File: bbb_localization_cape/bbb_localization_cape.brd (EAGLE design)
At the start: 71.8 x 54.6 mm, 33 parts, among them J2 MOLEX-22-03-5035, U1 SN65HVD256DR, U2 ARDUCAMOV5642, U3 SN74LV1T126DCKR, U4 MSP430G2553IPW20R, U5 SN74LV1T125DCKR, U6 LP38693MP-3.3/NOPB, U7 LM1085ISX-ADJ

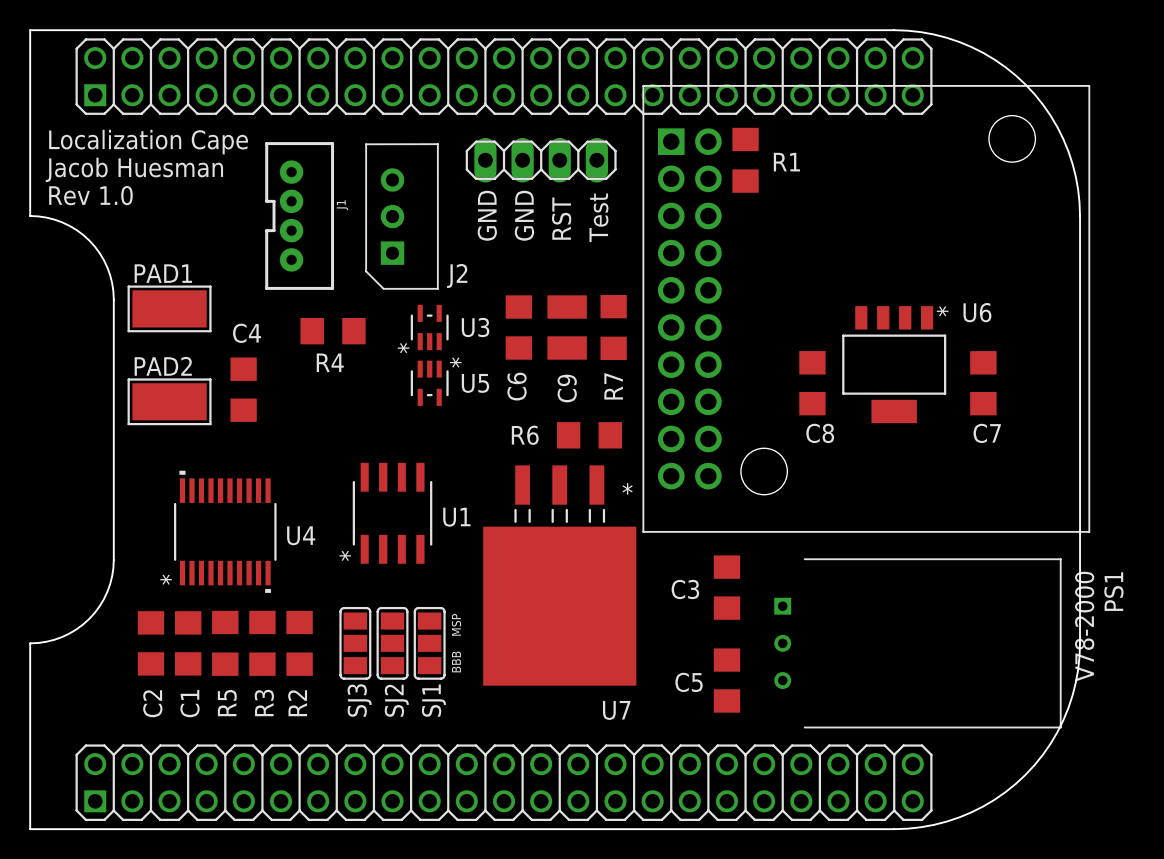
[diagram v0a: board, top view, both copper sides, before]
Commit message: Create ground plane
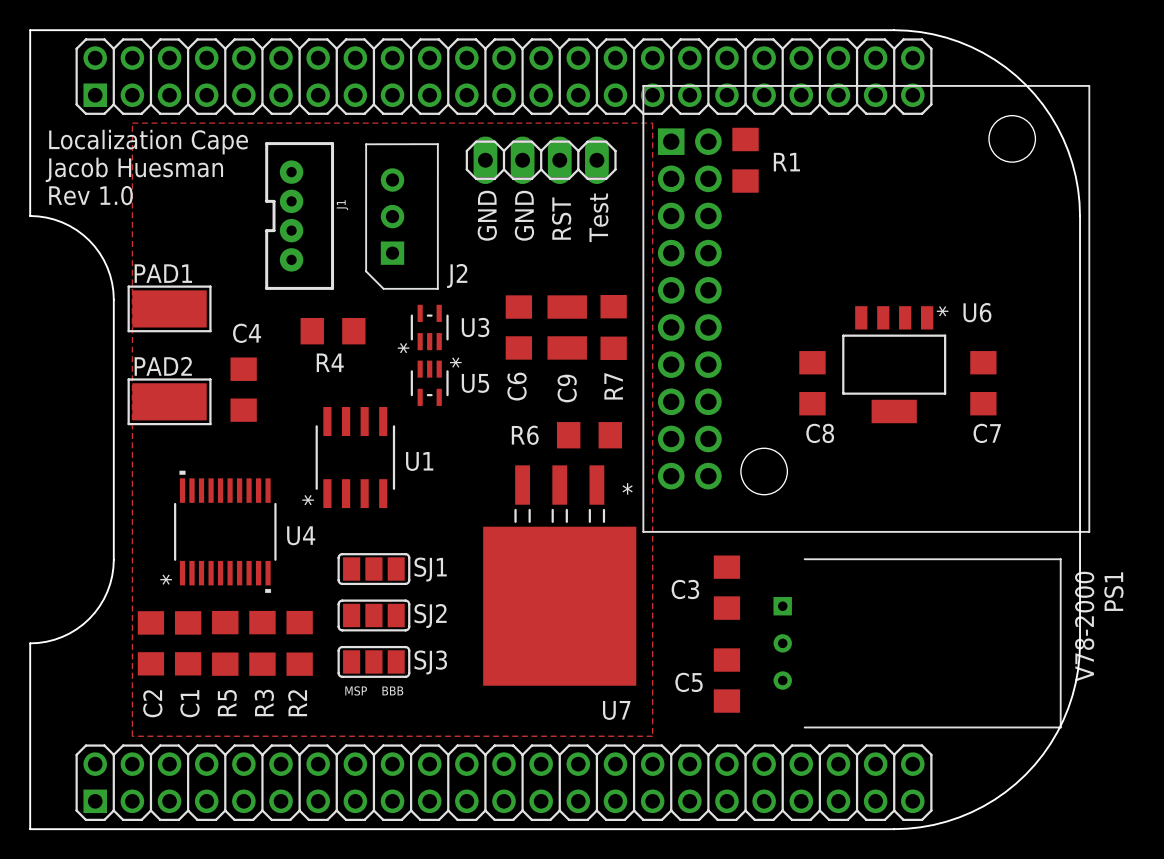
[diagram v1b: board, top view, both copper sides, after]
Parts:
- moved SJ1 6.35 mm to (38.1, 17.8), turned to 0 degrees
- moved U1 4.58 mm to (36.8, 25.4)
- moved SJ2 2.29 mm to (38.1, 14.6), turned to 0 degrees
- moved SJ3 1.80 mm to (38.1, 11.4), turned to 0 degrees
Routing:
- added copper zone on layer 1, net GND

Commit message: Laid out power connections
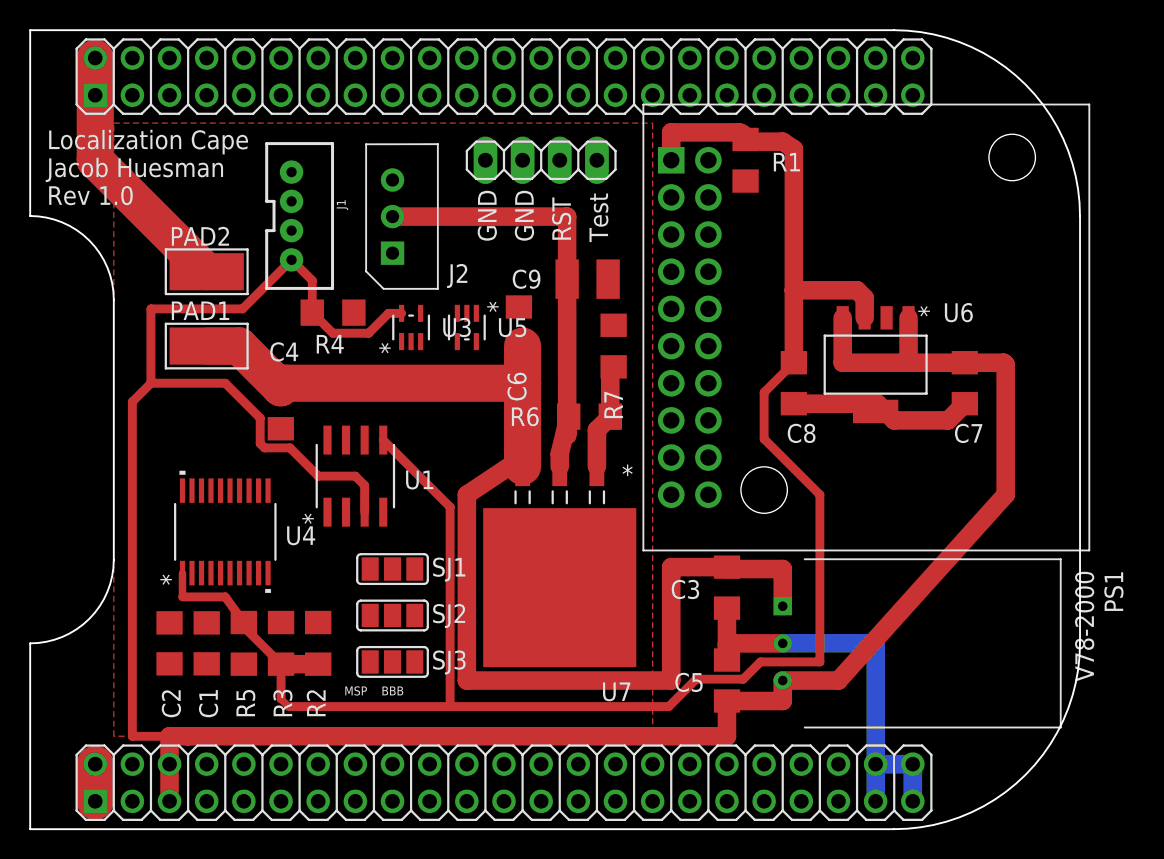
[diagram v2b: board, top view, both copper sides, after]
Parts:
- moved PAD2 9.25 mm to (26.7, 38.1)
- moved U5 4.58 mm to (44.5, 34.3)
- moved PAD1 3.59 mm to (26.7, 33.0)
- moved C9 3.59 mm to (52.7, 37.6), turned to 0 degrees
- moved C4 2.84 mm to (31.7, 28.8)
- moved C1 1.27 mm to (26.7, 12.7)
- moved U2 1.27 mm to (58.4, 45.7)
- moved U7 1.27 mm to (50.8, 16.5)
- moved C2 1.27 mm to (24.1, 12.7)
- moved R3 1.27 mm to (31.8, 12.7)
- moved R5 1.27 mm to (29.2, 12.7)
- moved R6 1.27 mm to (52.8, 28.2)
- moved U1 1.27 mm to (36.8, 24.1)
- moved C7 1.27 mm to (78.5, 30.5)
- moved C8 1.27 mm to (66.8, 30.5)
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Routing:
- net +5V: track 0.00 -> 173.6 mm
- net +3V3: track 0.00 -> 128.6 mm
- net +12V: track 0.00 -> 80.4 mm
- net GND: track 0.00 -> 63.7 mm
- net +10V: track 0.00 -> 31.6 mm
- net N$3: track 0.00 -> 7.28 mm

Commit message: Finished board layout
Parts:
- moved R1 17.5 mm to (79.7, 39.1), turned to 0 degrees
- moved C7 3.81 mm to (82.3, 30.5)
- moved U6 3.81 mm to (76.2, 31.8)
- moved C8 3.81 mm to (70.6, 30.5)
- moved R7 1.27 mm to (55.8, 33.0)
- renumbered PAD1 to GND, PAD2 to +12V
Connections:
- new net N$4: C7.2, C8.2, U6.5
- net GND: no longer C7.2, C8.2, U6.5
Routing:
- net GND: track 63.7 -> 174.7 mm, vias 0 -> 8
- net I2C_SDA: track 0.00 -> 92.1 mm, vias 0 -> 3
- net I2C2_SCL: track 0.00 -> 78.7 mm, vias 0 -> 2
- net RST: track 0.00 -> 73.8 mm, vias 0 -> 3
- net DCAN1_TX: track 0.00 -> 53.1 mm, vias 0 -> 1
- net TEST: track 0.00 -> 52.0 mm, vias 0 -> 2
- net TIMER4: track 0.00 -> 50.3 mm
- net +3V3: track 128.6 -> 178.6 mm
- net PRU1_1: track 0.00 -> 37.3 mm
- net PRU1_0: track 0.00 -> 33.1 mm
- net PWDN: track 0.00 -> 32.6 mm
- net PRU1_3: track 0.00 -> 31.6 mm
- net PRU1_6: track 0.00 -> 29.2 mm, vias 0 -> 1
- net UART_DYN_RXD: track 0.00 -> 28.8 mm, vias 0 -> 2
- net PRU1_5: track 0.00 -> 28.0 mm
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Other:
- board text added: "Localization Cape Rev 1.0 JH"
- board text removed: "Localization Cape Jacob Huesman Rev 1.0"

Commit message: Fixed issues between board and schematic, had to ripup the board
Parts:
- moved +12V 5.08 mm to (26.7, 33.0)
- moved GND 5.08 mm to (26.7, 38.1)
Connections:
- removed net I2C2_SCL: A1.65, R1.1, U2.3
- removed net N$4: C7.2, C8.2, U6.5
- removed net TAB: U7.4
- net +10V: now also U7.4
- net +12V: now also +12V.1; no longer GND.1
- net GND: now also C7.2, C8.2, GND.1, U6.5; no longer +12V.1
- net I2C_SCL: now also A1.65, R1.1, U2.3
- net PRU1_12: now also A1.21
- net UART2_DIR: now also A1.69
- net UART_MSP_DIR: now also U4.8
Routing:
- net +3V3: track 178.6 -> 0.00 mm
- net +5V: track 176.4 -> 0.00 mm
- net GND: track 174.7 -> 0.00 mm, vias 8 -> 0
- net I2C_SDA: track 92.1 -> 0.00 mm, vias 3 -> 0
- net +12V: track 80.8 -> 0.00 mm
- net I2C2_SCL: track 78.7 -> 0.00 mm, vias 2 -> 0
- net RST: track 73.8 -> 0.00 mm, vias 3 -> 0
- net DCAN1_TX: track 53.1 -> 0.00 mm, vias 1 -> 0
- net TEST: track 52.0 -> 0.00 mm, vias 2 -> 0
- net TIMER4: track 50.3 -> 0.00 mm
- net PRU1_1: track 37.3 -> 0.00 mm
- net PRU1_0: track 33.1 -> 0.00 mm
- net PWDN: track 32.6 -> 0.00 mm
- net +10V: track 31.6 -> 0.00 mm
- net PRU1_3: track 31.6 -> 0.00 mm
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
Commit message: Cleaned up beaglebone_outline schematic symbol
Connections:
- net I2C_SCL renamed I2C2_SCL
- net I2C_SDA renamed I2C2_SDA
- net SYS_5V renamed 07.SYS_5V
- removed net AIN0: A1.85
- removed net VDD_3V3EXP: A1.49, A1.50
- new net 03.VDD_3V3: A1.49
- new net GNDA_ADC.34: A1.80
- new net SYS_5V.08: A1.54
- new net VDD_3V3.04: A1.50
- new net VDD_ADC.32: A1.78
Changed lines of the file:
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@@
 <signals>
 <signal name="SYS_5V">
-<contactref element="A1" pad="53"/>
 </signal>
 <signal name="AIN0">
-<contactref element="A1" pad="85"/>
 </signal>
 <signal name="GND">
@@
 <contactref element="JP1" pad="4"/>
 <contactref element="JP1" pad="3"/>
-<contactref element="A1" pad="89"/>
-<contactref element="A1" pad="90"/>
-<contactref element="A1" pad="91"/>
-<contactref element="A1" pad="92"/>
-<contactref element="A1" pad="1"/>
-<contactref element="A1" pad="2"/>
 <contactref element="U1" pad="2"/>
 <contactref element="J1" pad="1"/>
@@
 <contactref element="U6" pad="5"/>
 <contactref element="C8" pad="2"/>
+<contactref element="A1" pad="1"/>
+<contactref element="A1" pad="2"/>
+<contactref element="A1" pad="89"/>
+<contactref element="A1" pad="91"/>
+<contactref element="A1" pad="90"/>
+<contactref element="A1" pad="92"/>
 <wire x1="76.2" y1="28.5496" x2="82.296" y2="29.08" width="0" layer="19" extent="1-1"/>
 <wire x1="70.612" y1="29.08" x2="76.2" y2="28.5496" width="0" layer="19" extent="1-1"/>
@@
 <wire x1="49.53" y1="4.445" x2="34.925" y2="21.6662" width="0" layer="19" extent="1-1"/>
 </signal>
-<signal name="I2C_SDA">
+<signal name="I2C2_SDA">
 <contactref element="A1" pad="66"/>
 <contactref element="U4" pad="15"/>
@@
 </signal>
 <signal name="VDD_3V3EXP">
-<contactref element="A1" pad="49"/>
-<contactref element="A1" pad="50"/>
-<wire x1="21.59" y1="1.905" x2="21.59" y2="4.445" width="0" layer="19" extent="1-1"/>
 </signal>
 <signal name="PRU1_8">
@@
 <wire x1="24.13" y1="11.3" x2="29.21" y2="11.278" width="0" layer="19" extent="1-1"/>
 </signal>
-<signal name="I2C_SCL">
+<signal name="I2C2_SCL">
 <contactref element="U4" pad="14"/>
 <contactref element="A1" pad="65"/>
@@
 <wire x1="36.195" y1="26.5938" x2="32.47" y2="40.91" width="0" layer="19" extent="1-1"/>
 </signal>
+<signal name="03.VDD_3V3">
+<contactref element="A1" pad="49"/>
+</signal>
+<signal name="07.SYS_5V">
+<contactref element="A1" pad="53"/>
+</signal>
+<signal name="39">
+</signal>
+<signal name="VDD_3V3.04">
+<contactref element="A1" pad="50"/>
+</signal>
+<signal name="SYS_5V.08">
+<contactref element="A1" pad="54"/>
+</signal>
+<signal name="VDD_ADC.32">
+<contactref element="A1" pad="78"/>
+</signal>
+<signal name="GNDA_ADC.34">
+<contactref element="A1" pad="80"/>
+</signal>
 </signals>

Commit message: Went over the entire schematic
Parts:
- removed C1: 100nF, resistor:C1206
- removed R3: 47k, resistor:R1206
- J2: device bbb_cape_parts:MOLEX-22-03-5035 -> bbb_localization_cape:MOLEX-22-03-5035
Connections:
- removed net N$7: C1.1, R3.1, U4.5
- net +3V3: no longer R3.2
- net GND: no longer C1.2
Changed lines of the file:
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@@
 <attribute name="VENDOR" value="Texas Instruments" x="27.94" y="20.32" size="1.778" layer="27" rot="R90" display="off"/>
-</element>
-<element name="R3" library="resistor" library_urn="urn:adsk.eagle:library:348" package="R1206" package3d_urn="urn:adsk.eagle:package:26062/1" value="47k" x="31.75" y="12.7" smashed="yes" rot="R270">
-<attribute name="NAME" x="31.242" y="9.652" size="1.27" layer="25" rot="R270"/>
-</element>
-<element name="C1" library="resistor" library_urn="urn:adsk.eagle:library:348" package="C1206" package3d_urn="urn:adsk.eagle:package:26140/1" value="100nF" x="26.67" y="12.7" smashed="yes" rot="R90">
-<attribute name="NAME" x="26.162" y="9.652" size="1.27" layer="25" rot="R270"/>
 </element>
 <element name="R5" library="resistor" library_urn="urn:adsk.eagle:library:348" package="R1206" package3d_urn="urn:adsk.eagle:package:26062/1" value="47k" x="29.21" y="12.7" smashed="yes" rot="R90">
@@
 <attribute name="NAME" x="34.036" y="32.512" size="1.27" layer="25"/>
 </element>
-<element name="J2" library="bbb_cape_parts" package="MOLEX-22-03-5035" value="MOLEX-22-03-5035" x="39.37" y="39.37" smashed="yes" rot="R90">
+<element name="J2" library="bbb_localization_cape" package="MOLEX-22-03-5035" value="MOLEX-22-03-5035" x="39.37" y="39.37" smashed="yes" rot="R90">
 <attribute name="NAME" x="43.18" y="37.338" size="1.27" layer="25"/>
 </element>
@@
 <contactref element="C9" pad="2"/>
 <contactref element="C6" pad="2"/>
-<contactref element="C1" pad="2"/>
 <contactref element="U4" pad="20"/>
 <contactref element="C2" pad="2"/>
@@
 <wire x1="25.015003125" y1="23.1394" x2="31.73415" y2="27.36826875" width="0" layer="19" extent="1-1"/>
 <wire x1="24.13" y1="14.1" x2="25.015003125" y2="23.1394" width="0" layer="19" extent="1-1"/>
-<wire x1="26.67" y1="14.1" x2="24.13" y2="14.1" width="0" layer="19" extent="1-1"/>
 <wire x1="19.05" y1="4.445" x2="24.13" y2="14.1" width="0" layer="19" extent="1-1"/>
 <wire x1="19.05" y1="1.905" x2="19.05" y2="4.445" width="0" layer="19" extent="1-1"/>
@@
 <contactref element="C8" pad="1"/>
 <contactref element="U6" pad="3"/>
-<contactref element="R3" pad="2"/>
 <contactref element="U4" pad="1"/>
 <contactref element="R5" pad="2"/>
@@
 <wire x1="38.735" y1="26.5938" x2="45.1" y2="33.3248" width="0" layer="19" extent="1-1"/>
 <wire x1="29.21" y1="14.122" x2="38.735" y2="26.5938" width="0" layer="19" extent="1-1"/>
-<wire x1="31.75" y1="11.278" x2="29.21" y2="14.122" width="0" layer="19" extent="1-1"/>
-<wire x1="34.29" y1="11.278" x2="31.75" y2="11.278" width="0" layer="19" extent="1-1"/>
 <wire x1="25.015" y1="17.5006" x2="29.21" y2="14.122" width="0" layer="19" extent="1-1"/>
+<wire x1="34.29" y1="11.278" x2="29.21" y2="14.122" width="0" layer="19" extent="1-1"/>
 </signal>
 <signal name="VDD_3V3EXP">
@@
 <wire x1="46.99" y1="1.905" x2="40.894" y2="17.78" width="0" layer="19" extent="1-1"/>
 </signal>
-<signal name="N$7">
-<contactref element="R3" pad="1"/>
-<contactref element="U4" pad="5"/>
-<contactref element="C1" pad="1"/>
-<wire x1="27.615" y1="17.5006" x2="31.75" y2="14.122" width="0" layer="19" extent="1-1"/>
-<wire x1="26.67" y1="11.3" x2="31.75" y2="14.122" width="0" layer="19" extent="1-1"/>
-</signal>
 <signal name="TEST">
